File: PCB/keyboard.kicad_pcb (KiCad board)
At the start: 2 copper layers, 150.9 x 123.7 mm, 57 parts, among them J1 AudioJack4, J2 Conn_01x02, J3 Conn_01x05, SW1 Switch+Diode, SW10 Switch+Diode, SW11 Switch+Diode, SW12 Switch+Diode, SW13 Switch+Diode, SW14 Switch+Diode, SW15 Switch+Diode, SW16 Switch+Diode, SW17 Switch+Diode, SW18 RotaryEncoder_Switch, SW19 Switch+Diode, SW2 Switch+Diode, SW20 Switch+Diode, SW21 Switch+Diode, SW22 Switch+Diode, SW23 Switch+Diode, SW24 SW_PUSH, SW25 SW_DPDT_x2, SW3 Switch+Diode, SW4 Switch+Diode, SW5 Switch+Diode, SW6 Switch+Diode, SW7 Switch+Diode, SW8 Switch+Diode, SW9 Switch+Diode, U1 nice!nano

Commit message: preliminary routing
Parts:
- D1, JP2, JP3: moved to B.Cu
- JP1, JP4, SW22, SW23: moved to F.Cu
- moved J2 75.8 mm to (108.8, 27.7), turned to 0 degrees
- moved D1 1.61 mm to (86.2, 101.7), turned to 0 degrees
- turned D8 to 160 degrees
- turned JP1 to 0 degrees
- turned JP2 to 0 degrees
- turned JP3 to 0 degrees
- turned JP4 to 0 degrees
- turned SW22 to -45 degrees
- turned SW23 to -70 degrees
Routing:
- net row3: track 0.00 -> 155.6 mm, vias 0 -> 5
- net col1: track 0.00 -> 152.6 mm, vias 0 -> 1
- net row0: track 0.00 -> 149.2 mm, vias 0 -> 5
- net row1: track 0.00 -> 134.9 mm, vias 0 -> 5
- net col5: track 0.00 -> 134.1 mm, vias 0 -> 1
- net row2: track 0.00 -> 122.5 mm, vias 0 -> 5
- net col0: track 0.00 -> 121.8 mm
- net col4: track 0.00 -> 95.9 mm
- net col3: track 0.00 -> 93.6 mm
- net CS: track 0.00 -> 88.4 mm, vias 0 -> 2
- net col2: track 0.00 -> 87.9 mm
- net RESET: track 0.00 -> 77.3 mm
- net GND: track 0.00 -> 76.7 mm, vias 0 -> 3
- net SDA: track 0.00 -> 64.5 mm, vias 0 -> 1
- net VCC: track 0.00 -> 63.2 mm, vias 0 -> 3
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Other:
- outline, holes or cut-outs redrawn

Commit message: 3d assets + bad routing
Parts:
- D7: moved to F.Cu
- moved J2 71.4 mm to (146.4, 88.4)
- moved D5 9.27 mm to (65.8, 65.4), turned to 135 degrees
- moved D4 4.41 mm to (85.5, 50.6), turned to 45 degrees
- moved D8 0.87 mm to (137.8, 98.3)
- moved D7 0.18 mm to (106.6, 95.9)
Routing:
- net col4: track 95.9 -> 179.7 mm, vias 0 -> 2
- net Net-(D4-Pad2): track 42.6 -> 0.00 mm
- net Net-(D6-Pad2): track 43.1 -> 4.18 mm
- net Net-(D3-Pad2): track 40.3 -> 4.18 mm, vias 1 -> 0
- net Net-(D5-Pad2): track 37.8 -> 4.18 mm
- net Net-(D7-Pad2): track 33.9 -> 4.25 mm
- net Net-(D2-Pad2): track 37.6 -> 8.36 mm, vias 1 -> 0
- net col5: track 134.1 -> 159.8 mm, vias 1 -> 2
- net GND: track 76.7 -> 52.6 mm, vias 3 -> 0
- net VCC: track 63.2 -> 41.1 mm, vias 3 -> 0
- net col0: track 121.8 -> 143.6 mm
- net col3: track 93.6 -> 114.6 mm
- net col1: track 152.6 -> 172.6 mm, vias 1 -> 0
- net SDA: track 64.5 -> 55.6 mm, vias 1 -> 0
- net SCK: track 31.6 -> 40.2 mm, vias 3 -> 1
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
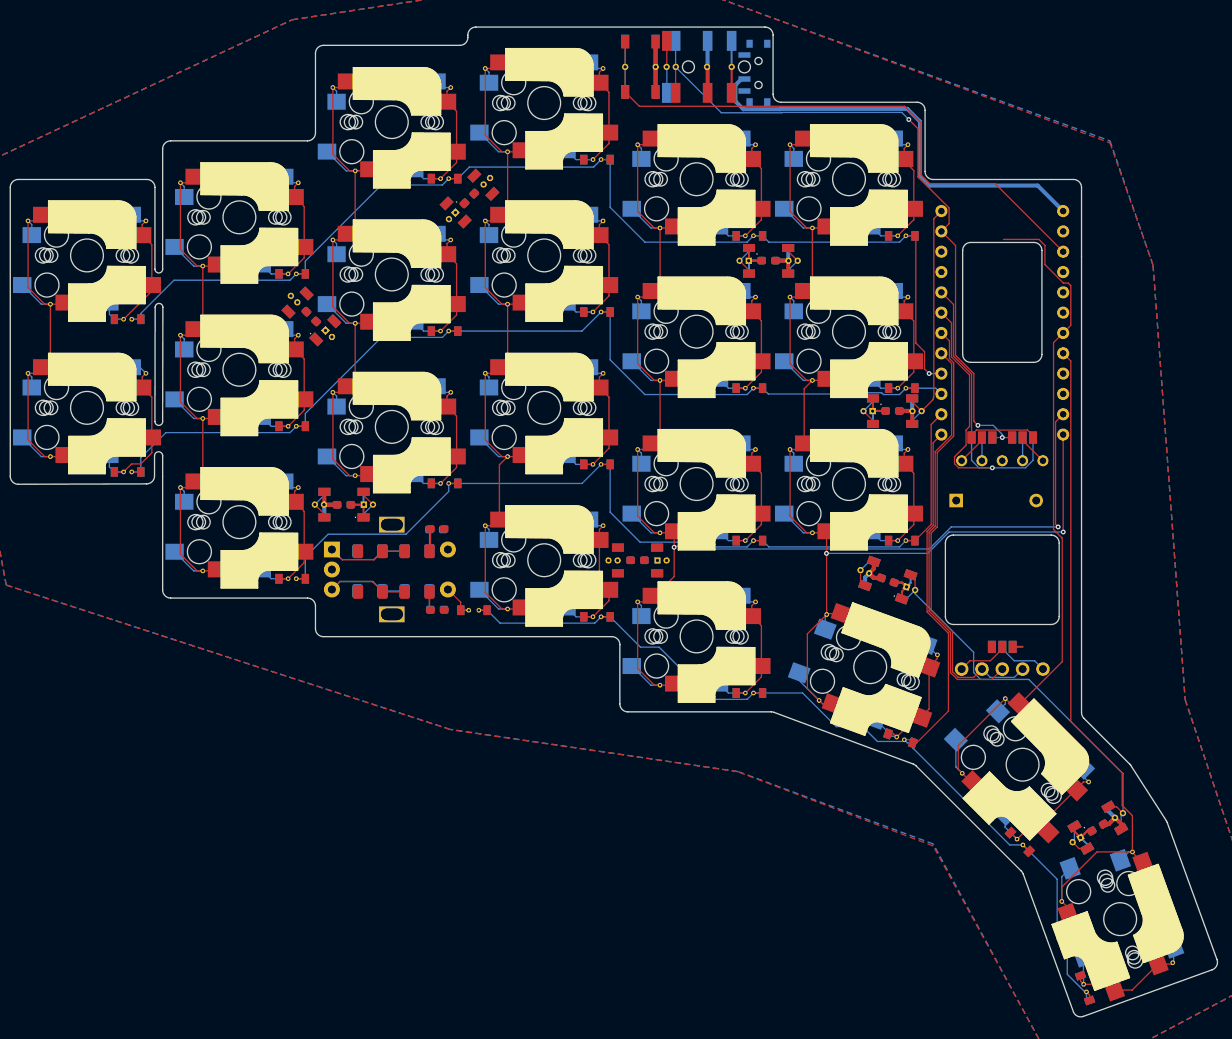
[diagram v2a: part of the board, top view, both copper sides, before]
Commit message: wired compatible/breakaway
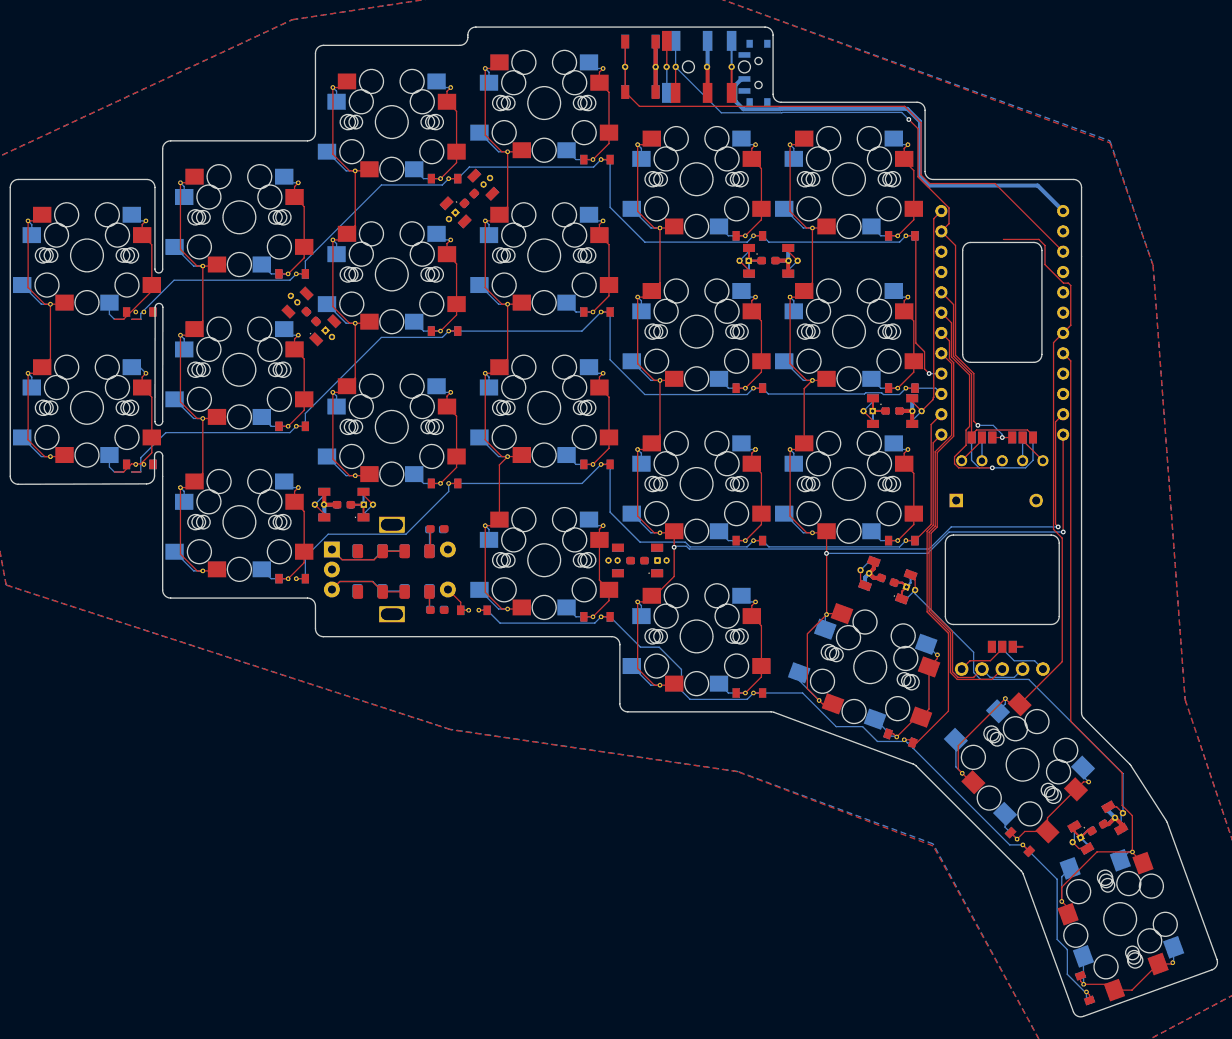
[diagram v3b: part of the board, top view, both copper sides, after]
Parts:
- D7: moved to B.Cu

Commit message: curvy traces
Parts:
- removed the C1 at (81.4, 92.0)
- removed the C2 at (81.5, 102.0)
- removed J1: AudioJack4, hb44:SMD_3.5mm_TRRS
- removed the R1 at (73.1, 94.7)
- removed the R2 at (73.1, 99.7)
- removed the R3 at (79.0, 94.7)
- removed the R4 at (79.0, 99.7)
- added H1: MountingHole, hb44:MountingHole_4mm, F.Cu at (65.0, 81.5)
- added H2: MountingHole, hb44:MountingHole_4mm, F.Cu at (147.4, 114.4)
- added H3: MountingHole, hb44:MountingHole_4mm, F.Cu at (113.9, 36.0)
- added Q1: Q_PMOS_GSD, Package_TO_SOT_SMD:SOT-23_Handsoldering, F.Cu at (152.0, 55.0)
- C1: renamed from C19; moved to B.Cu
- C2: renamed from C20; moved to B.Cu
- R1: renamed from R5; moved to B.Cu
- R2: renamed from R6; moved to B.Cu
- R3: renamed from R7; moved to B.Cu
- R4: renamed from R8; moved to B.Cu
- SW24: footprint hb44:SMD_SW_PUSH -> hb44:SMD_SW_SPST_B3U-3000P-B; moved to B.Cu
- SW25: footprint Button_Switch_SMD:SW_SPDT_PCM12 -> hb44:SMD_SW_SPDT_PCM12
- U1: moved to F.Cu
- moved SW25 12.9 mm to (108.9, 31.6), turned to 0 degrees
- moved SW24 12.6 mm to (118.9, 30.6), turned to 180 degrees
- moved C1 11.2 mm to (84.1, 102.9)
- moved J2 11.1 mm to (157.2, 86.1), turned to 180 degrees
- moved C2 11.0 mm to (84.1, 91.4)
- moved D6 8.72 mm to (78.4, 87.0)
- moved SW18 7.94 mm to (75.8, 97.2), turned to 180 degrees
- moved D4 7.23 mm to (92.3, 48.1), turned to 0 degrees
- moved D2 7.05 mm to (132.9, 72.8)
- moved R4 6.81 mm to (80.3, 93.1), turned to 90 degrees
- moved R3 6.74 mm to (80.3, 101.3), turned to -90 degrees
- moved R1 5.81 mm to (75.9, 99.8)
- moved R2 5.74 mm to (75.8, 94.7)
- moved D7 5.21 mm to (110.9, 93.0)
- moved D3 4.58 mm to (121.2, 54.2)
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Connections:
- net Net-(J2-Pad2) renamed /RAW_BAT
- D1 pad 2: rotS1 -> rotS2
- D2 pad 1: VCC -> /LED_VCC
- D2 pad 4: LED -> ARGB
- D3 pad 1: VCC -> /LED_VCC
- D4 pad 1: VCC -> /LED_VCC
- D5 pad 1: VCC -> /LED_VCC
- D6 pad 1: VCC -> /LED_VCC
- D7 pad 1: VCC -> /LED_VCC
- D8 pad 1: VCC -> /LED_VCC
- D9 pad 1: VCC -> /LED_VCC
- SW18 pad S1: rotS1 -> col2
- SW18 pad S2: col2 -> rotS2
- SW22 pad 1: col0 -> col1
- SW23 pad 1: col1 -> col0
- U1 pad 1: LED -> ARGB
- U1 pad 10: row1 -> SCK
- U1 pad 11: row2 -> unconnected-(U1-Pad11)
- U1 pad 12: row3 -> rotA
- U1 pad 13: col5 -> row3
- U1 pad 14: col4 -> row2
- U1 pad 19: rotB -> row1
- U1 pad 2: CS -> LED
- U1 pad 20: rotA -> row0
- U1 pad 5: MOSI -> CS
- U1 pad 6: SCK -> MOSI
- U1 pad 7: SDA -> unconnected-(U1-Pad7)
- U1 pad 8: SCL -> SDA
- U1 pad 9: row0 -> SCL
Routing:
- net /LED_VCC: track 0.00 -> 325.2 mm, vias 0 -> 10
- net VCC: track 41.1 -> 160.8 mm, vias 0 -> 4
- net col0: track 143.6 -> 245.7 mm
- net rotA: track 5.55 -> 101.0 mm, vias 0 -> 2
- net /RAW_BAT: track 0.00 -> 91.5 mm, vias 0 -> 6
- net rotB: track 4.68 -> 82.8 mm, vias 0 -> 1
- net col2: track 83.8 -> 150.7 mm, vias 0 -> 1
- net col4: track 179.7 -> 120.6 mm, vias 2 -> 1
- net col1: track 172.6 -> 231.3 mm
- net CS: track 87.4 -> 29.0 mm, vias 3 -> 0
- net col5: track 159.8 -> 101.9 mm, vias 2 -> 1
- net ARGB: track 0.00 -> 39.9 mm, vias 0 -> 1
- net Net-(D5-Pad2): track 4.18 -> 42.1 mm, vias 0 -> 1
- net Net-(D4-Pad2): track 0.00 -> 34.9 mm
- net Net-(D6-Pad2): track 4.18 -> 38.4 mm, vias 0 -> 2
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- added copper zone on F.Cu, net GND
- removed copper zone on F.Cu, net VCC
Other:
- outline, holes or cut-outs redrawn
- board text added: "-transistor reversible -led positions margin"
- board text added: "hb44 - designed by nandrew"
- board text removed: "失 恋"

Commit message: working 44
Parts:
- Q1: footprint Package_TO_SOT_SMD:SOT-23_Handsoldering -> hb44:SMD_P_MOSTFET_SOT-23
- moved H1 0.87 mm to (65.9, 81.6)
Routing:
- net Net-(D5-Pad2): track 42.1 -> 60.8 mm, vias 1 -> 3
- net VCC: track 160.8 -> 169.2 mm
- net /LED_VCC: track 325.2 -> 327.2 mm
- net LED: track 7.10 -> 9.01 mm, vias 0 -> 1
- net ARGB: track 39.9 -> 40.5 mm
- net GND: vias 49 -> 51
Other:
- outline, holes or cut-outs redrawn
- board text added: "-led cap positions margin -mosfet gate resistors? -peel a way sockets -finger print position"
- board text removed: "-transistor reversible -led positions margin"

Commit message: reversible WIP
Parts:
- removed D2, D3, D4, D5, D6, D7, D8, D9: WS2812B+Cap, hb44:SMD_WS2812B+Cap0603
- removed the SW1 at (37.7, 57.8)
- removed the SW7 at (37.7, 76.8)
- added LED1: 0.1u, hb44:SK6812-SIDE + 1608m Cap, F.Cu at (159.6, 52.7)
- added LED10: 0.1u, hb44:SK6812-SIDE + 1608m Cap, F.Cu at (131.5, 147.4)
- added LED11: 0.1u, hb44:SK6812-SIDE + 1608m Cap, F.Cu at (119.2, 142.5)
- added LED12: 0.1u, hb44:SK6812-SIDE + 1608m Cap, F.Cu at (126.4, 147.4)
- added LED13: 0.1u, hb44:SK6812-SIDE + 1608m Cap, F.Cu at (131.8, 153.3)
- added LED14: 0.1u, hb44:SK6812-SIDE + 1608m Cap, F.Cu at (121.6, 153.3)
- added LED15: 0.1u, hb44:SK6812-SIDE + 1608m Cap, F.Cu at (124.3, 142.5)
- added LED16: 0.1u, hb44:SK6812-SIDE + 1608m Cap, F.Cu at (126.7, 153.3)
- added LED17: 0.1u, hb44:SK6812-SIDE + 1608m Cap, F.Cu at (119.2, 137.2)
- added LED18: 0.1u, hb44:SK6812-SIDE + 1608m Cap, F.Cu at (134.5, 137.2)
- added LED19: 0.1u, hb44:SK6812-SIDE + 1608m Cap, F.Cu at (124.3, 137.2)
- added LED2: 0.1u, hb44:SK6812-SIDE + 1608m Cap, F.Cu at (159.6, 70.7)
- added LED20: 0.1u, hb44:SK6812-SIDE + 1608m Cap, F.Cu at (134.5, 142.5)
- added LED21: 0.1u, hb44:SK6812-SIDE + 1608m Cap, F.Cu at (129.4, 137.2)
- added LED22: 0.1u, hb44:SK6812-SIDE + 1608m Cap, F.Cu at (121.3, 147.4)
- added LED3: 0.1u, hb44:SK6812-SIDE + 1608m Cap, F.Cu at (109.9, 125.3)
- added LED4: 0.1u, hb44:SK6812-SIDE + 1608m Cap, F.Cu at (115.4, 125.5)
- added LED5: 0.1u, hb44:SK6812-SIDE + 1608m Cap, F.Cu at (121.9, 125.4)
- added LED6: 0.1u, hb44:SK6812-SIDE + 1608m Cap, F.Cu at (128.8, 125.3)
- added LED7: 0.1u, hb44:SK6812-SIDE + 1608m Cap, F.Cu at (134.0, 125.2)
- added LED8: 0.1u, hb44:SK6812-SIDE + 1608m Cap, F.Cu at (139.7, 128.7)
- added LED9: 0.1u, hb44:SK6812-SIDE + 1608m Cap, F.Cu at (129.4, 142.5)
- added R5: 200, hb44:SMD_Res_1206, F.Cu at (168.2, 69.7)
- added R6: 200k, hb44:SMD_Res_1206, F.Cu at (166.6, 63.8)
- added U2: 74AUP2G14, Package_TO_SOT_SMD:SOT-363_SC-70-6_Handsoldering, F.Cu at (75.0, 110.1)
- C1, C2: value 10n -> 0.1u
- J3: moved to F.Cu
- SW15: renamed from SW17; moved to B.Cu
- SW5: renamed from SW6; moved to B.Cu
- U1: value nice!nano -> ProMicro_r
- moved H2 129.4 mm to (42.7, 38.5)
- moved H3 57.8 mm to (56.1, 35.9)
- moved H1 56.0 mm to (32.3, 36.8)
- moved Q1 26.9 mm to (176.4, 66.3), turned to 0 degrees
- moved J2 24.3 mm to (178.2, 98.3)
- moved JP1 21.6 mm to (169.7, 88.5)
- moved JP2 21.0 mm to (170.4, 84.0)
- moved JP6 16.5 mm to (168.4, 103.8)
- moved JP5 16.3 mm to (168.4, 106.5)
- moved JP3 15.4 mm to (170.0, 81.3)
- moved JP4 15.1 mm to (169.5, 77.6)
- moved U1 2.80 mm to (149.4, 66.6)
- moved LCD1 1.45 mm to (150.7, 83.1)
- moved J3 1.42 mm to (150.7, 98.9), turned to 0 degrees
- turned SW10 to 90 degrees
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- renumbered SW2 to SW1, SW12 to SW10, SW13 to SW11, SW14 to SW12, SW15 to SW13, SW16 to SW14, SW18 to SW16, SW19 to SW17, SW20 to SW18, SW21 to SW19, SW3 to SW2, SW22 to SW20, SW23 to SW21, SW4 to SW3, SW5 to SW4, SW8 to SW6, SW9 to SW7, SW10 to SW8, SW11 to SW9
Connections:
- C1 pad 1: rotA -> Net-(C1-Pad1)
- C2 pad 1: rotB -> Net-(C2-Pad1)
- Q1 pad 1: LED -> Net-(Q1-Pad1)
- Q1 pad 2: /LED_VCC -> VCC
- Q1 pad 3: VCC -> /LED_VCC
- R3 pad 2: rotA -> Net-(C1-Pad1)
- R4 pad 2: rotB -> Net-(C2-Pad1)
- U1 pad 10: SCK -> col5
- U1 pad 11: unconnected-(U1-Pad11) -> rotB
- U1 pad 27: rotB -> col4
- U1 pad 7: unconnected-(U1-Pad7) -> SCK
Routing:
- net /LED_VCC: track 327.2 -> 0.00 mm, vias 10 -> 0
- net col0: track 245.7 -> 0.00 mm
- net col1: track 231.3 -> 49.7 mm
- net VCC: track 169.2 -> 10.2 mm, vias 4 -> 1
- net row3: track 149.3 -> 4.34 mm, vias 1 -> 0
- net row0: track 140.3 -> 6.80 mm
- net row1: track 124.3 -> 6.80 mm
- net col5: track 101.9 -> 0.00 mm, vias 1 -> 0
- net rotA: track 101.0 -> 0.00 mm, vias 2 -> 0
- net row2: track 99.0 -> 4.54 mm
- net rotB: track 82.8 -> 0.00 mm, vias 1 -> 0
- net /RAW_BAT: track 91.4 -> 9.29 mm, vias 6 -> 1
- net col2: track 150.7 -> 69.6 mm, vias 1 -> 0
- net col4: track 120.6 -> 49.7 mm, vias 1 -> 0
- net Net-(D5-Pad2): track 60.8 -> 0.00 mm, vias 3 -> 0
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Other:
- board size 150.9 x 123.7 mm -> 131.8 x 123.7 mm
- board text added: "heartbreak - designed by drew"
- board text removed: "-led cap positions margin -mosfet gate resistors? -peel a way sockets -finger print position"
- board text removed: "hb44 - designed by nandrew"
